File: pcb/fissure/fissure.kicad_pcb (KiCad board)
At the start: 2 copper layers, 213.5 x 98.2 mm, 64 parts, among them J1 Conn_01x04_Female, J2 USB_C_Receptacle_USB2.0, J3 Conn_01x06, J4 Conn_01x06, J5 OLED, J6 Conn_01x06, J7 Conn_01x06, K1 KEY, K10 KEY, K11 KEY, K12 KEY, K13 KEY, K14 KEY, K15 KEY, K16 KEY, K17 KEY, K18 KEY, K19 KEY, K2 KEY, K20 KEY, K3 KEY, K4 KEY, K5 KEY, K6 KEY, K7 KEY, K8 KEY, K9 KEY, Q1 AO3401A, Q2 AO3401A, SW1 SW_Push, SW2 SW_Push, SW3 SW_SPDT, SW4 SW_SPDT, U1 Holyiot_18010, U2 MT25QL128ABA1ESE, U3 LTC4054ES5-4.2, U4 MCP1700-3302E_SOT23

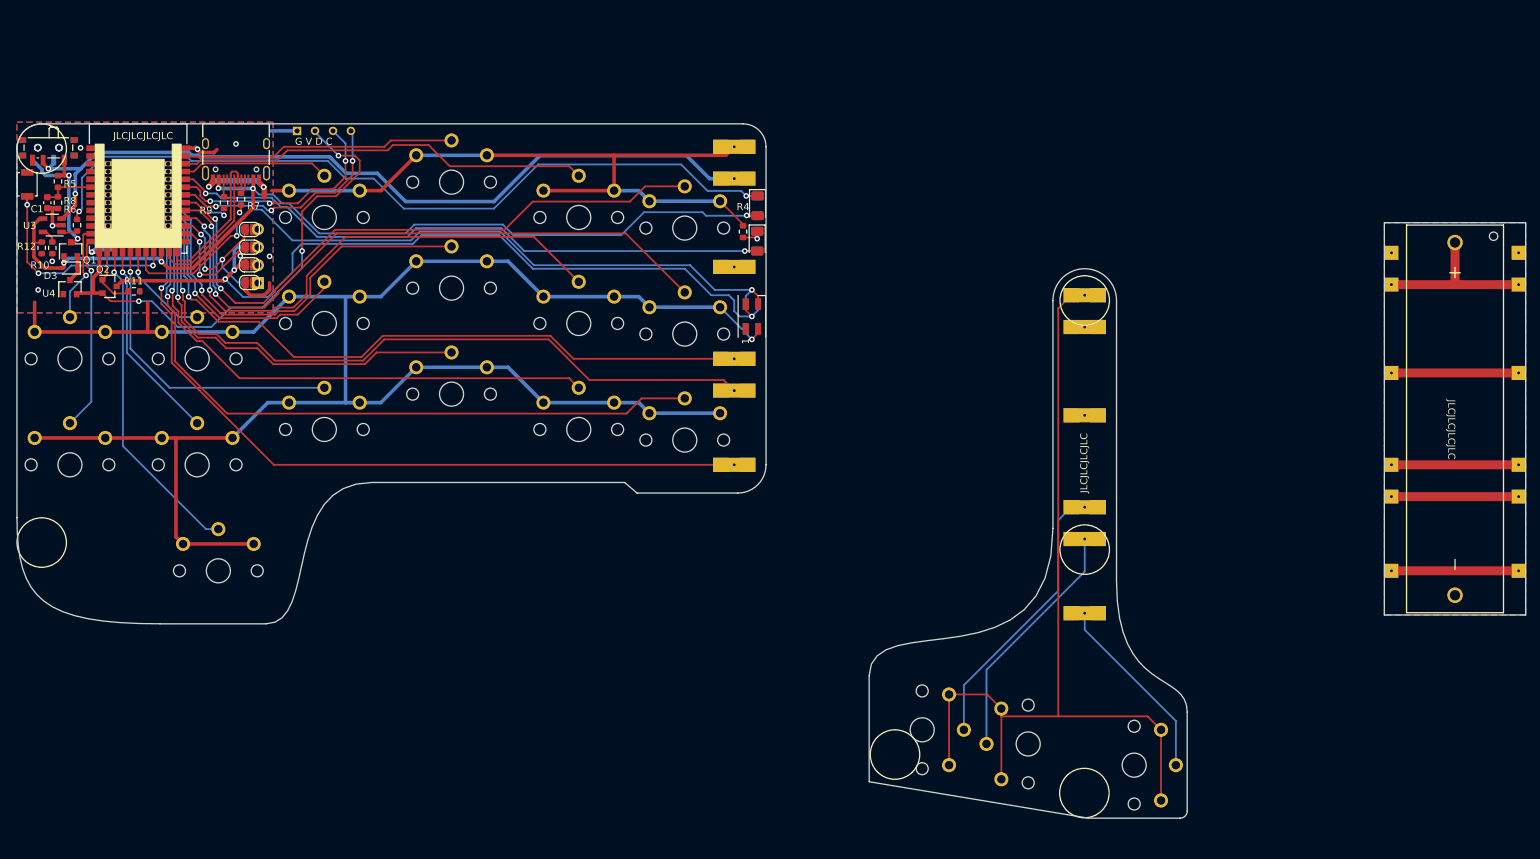
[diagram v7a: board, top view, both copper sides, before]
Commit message: stagger update
- middle 2 mm up
- outer index flat with home
- narrower pinky columns
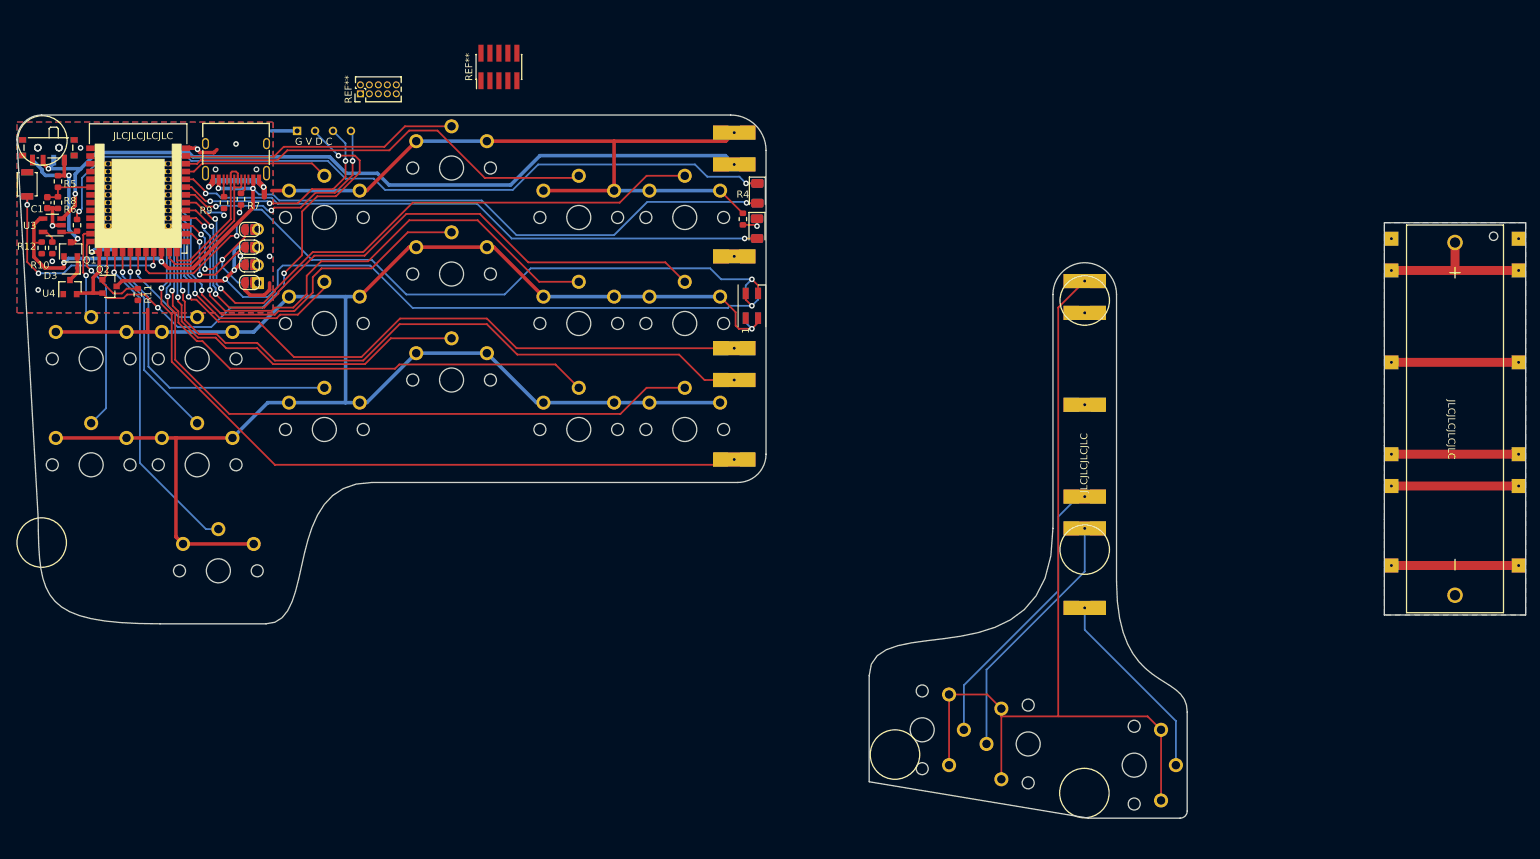
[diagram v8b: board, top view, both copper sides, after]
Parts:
- added REF**: PinHeader_2x05_P1.27mm_Vertical, Connector_PinHeader_1.27mm:PinHeader_2x05_P1.27mm_Vertical, F.Cu at (74.6, 52.0)
- added REF**: PinHeader_2x05_P1.27mm_Vertical_SMD, Connector_PinHeader_1.27mm:PinHeader_2x05_P1.27mm_Vertical_SMD, F.Cu at (94.2, 48.2)
- K1, K6: footprint pg1350:PG1350-reversible-no-diode-short -> pg1350:PG1350-reversible-no-diode-short-offcenter-outer
- K16, K17: footprint pg1350:PG1350-reversible-no-diode-short -> pg1350:PG1350-reversible-no-diode-short-offcenter
- moved K16 3.00 mm to (36.5, 89.5)
- moved K17 3.00 mm to (36.5, 104.5)
- moved K13 2.00 mm to (87.5, 92.5)
- moved K3 2.00 mm to (87.5, 62.5)
- moved K8 2.00 mm to (87.5, 77.5)
- moved R4 1.78 mm to (128.7, 69.7)
- moved D1 1.78 mm to (130.7, 71.1)
- moved D2 1.78 mm to (130.8, 66.1)
- moved D4 1.78 mm to (130.7, 71.1)
- moved D5 1.78 mm to (130.8, 66.1)
- moved D41 1.50 mm to (130.0, 82.0)
- moved D42 1.50 mm to (130.0, 82.0)
- moved K10 1.50 mm to (120.5, 84.5)
- moved K15 1.50 mm to (120.5, 99.5)
- moved K5 1.50 mm to (120.5, 69.5)
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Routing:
- net EXT_VCC: track 114.6 -> 109.6 mm
- net GND: track 404.5 -> 400.0 mm
- net Net-(D2-Pad1): track 112.1 -> 109.1 mm
- net BAT: track 116.3 -> 113.5 mm
- net bridge_BAT: track 24.0 -> 22.0 mm
- net K9: track 74.8 -> 76.8 mm
- net K4: track 58.5 -> 60.4 mm
- net BLUE: track 87.7 -> 85.9 mm
- net VCC_SWITCH: track 8.96 -> 10.5 mm
- net thumb_K19: track 34.8 -> 36.3 mm
- net RGB: track 103.7 -> 105.1 mm
- net K20: track 96.1 -> 97.5 mm
- net K10: track 89.8 -> 91.2 mm
- net K19: track 99.1 -> 100.3 mm
- net thumb_K20: track 39.7 -> 40.6 mm
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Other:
- board size 213.5 x 98.2 mm -> 213.5 x 99.5 mm
